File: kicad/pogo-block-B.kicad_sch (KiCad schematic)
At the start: 12 parts, among them J29 MAIN_L, J30 MAIN_R, U61 TL072, U62 TL072

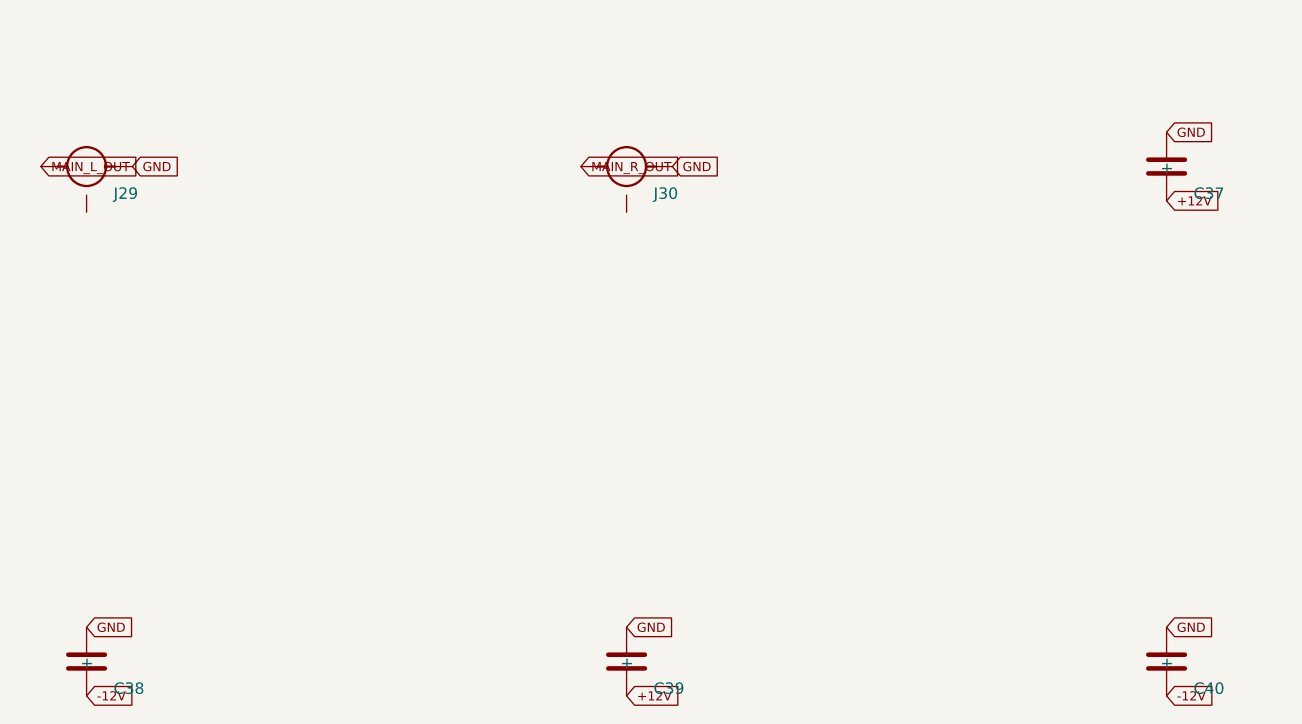
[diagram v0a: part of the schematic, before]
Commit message: 0015-component-audit: apply component verification fixes
Board-breaking:
- that2180: real MPN THAT2180AL08-U (grade A) + package SIP-8 (THT); vendor
  Package_SIP/SIP-8_2.54mm footprint; fix components.yaml U4/U5 + CLAUDE.md.
  The 2180 has no SMD/SOIC variant.
- bat54s: redraw symbol to real series topology (1=A1, 2=K2, 3=K1;A2 junction);
  swap pins 2<->3 on all 24 BAT54S instances (blocks A/1/3/4) so signal sits on the
  junction (pin3), +12V on K2 (pin2), -12V on A1 (pin1); fix aux-cv-protection.md +
  block-A spec (both mislabeled the signal node as pin 2).

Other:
- R_INV_IN/R_INV_FB: add tol 1% (header-required >60 dB null).
- slide_pot_45mm: MPN RA4522F (Alpha 45mm, Rapid/Banzai); fix datasheet link.
- bzx84c10: add shared BZX84_SER datasheet (committed PDF + sha256); canonical MPN.
- opa1612: add symbol opamp2. bourns_3296w/3224w: fix version strings.
- cd4053 symbol doc# -> SCHS047O; c.yaml pin1 '+' -> '~' (non-polarized).

Jack S/T/TN reconciliation deferred (its own change). Plugin DSP untouched.
Regenerated all schematics, BOM, fp-lib-table, footprint SVGs, panel; 5 gates green.
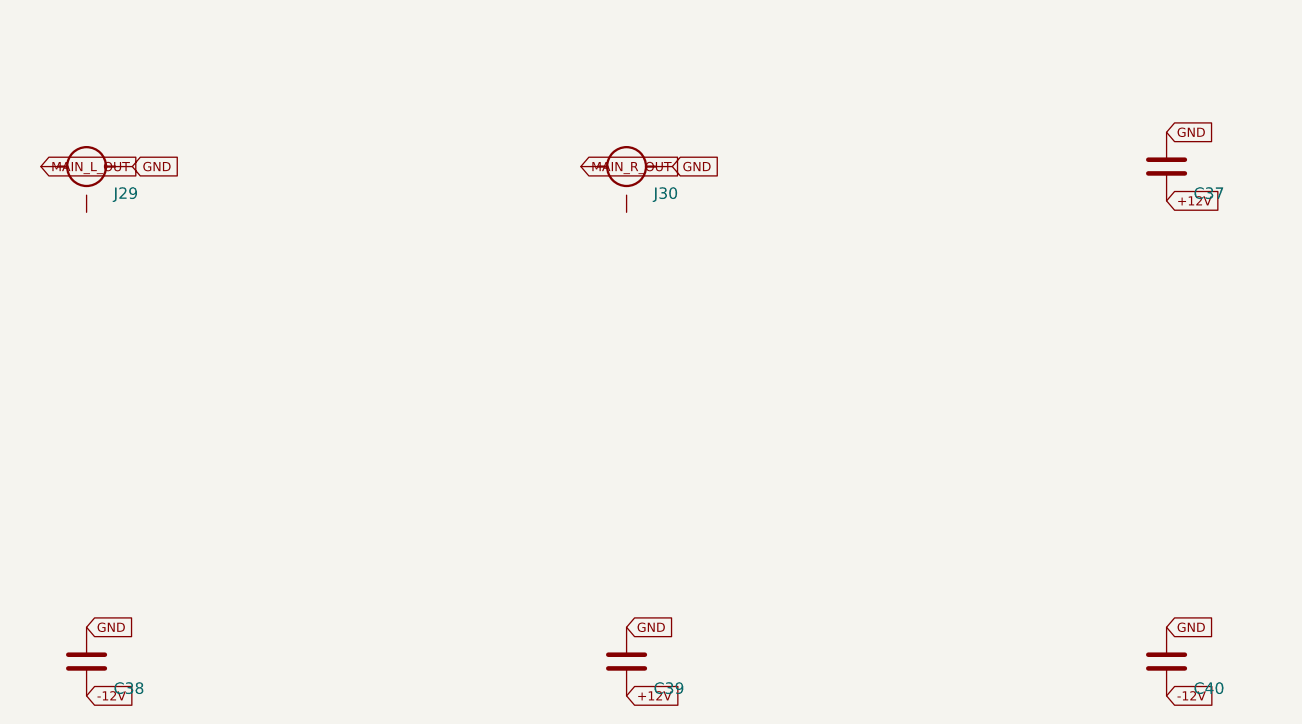
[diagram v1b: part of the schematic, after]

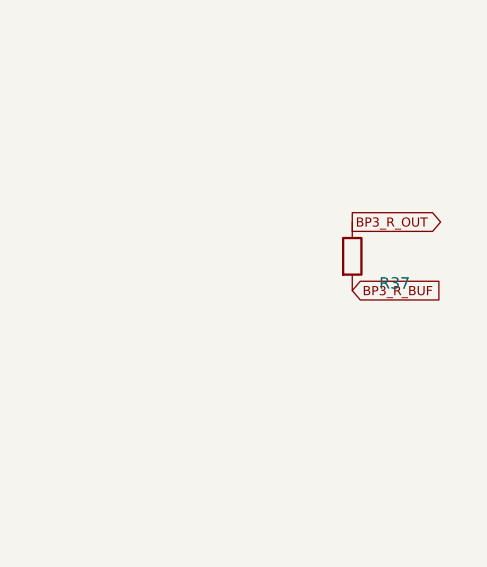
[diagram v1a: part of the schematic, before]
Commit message: 0018: block-B output buffers aligned to plugin (BP3_R normal + hygiene)
Final block. Adversarial review confirmed MAIN outputs faithful (non-inverting
unity followers, 1k series, +-11V via TL072 swing = plugin clamp, like block-A)
and the BP3 tap point correct (svf3 v1, post-bandpass/pre-mix). One real gap:
- BP3_R OUTPUT NORMALLING added: the plugin outputs BP3_L when the BP3_R jack
  is unpatched (Pogo.cpp:498-499). Wired J28.3 (switch lug) -> BP3_L_OUT in
  block-6-mix (which owns the BP3 jacks): BP3_L_OUT: [J27.1, J28.3], J28.3
  removed from no_connect. Mirrors block-A's L->R input normal.
- Renumbered block-B R37 -> R224 to clear the cross-block R37 collision with
  block-3's CV-protection resistors.
- Lifted §2/§3 STALE banners; fixed aux-unity-buffer refs (.svg/.md); noted the
  LFO output resistors are block-2 (utility), editorial in block-B.

All 10 blocks now aligned to the locked plugin. All 5 --check gates + parity green.

https://claude.ai/code/session_013jFXG5oeMVSYP7iRpwGvtQ
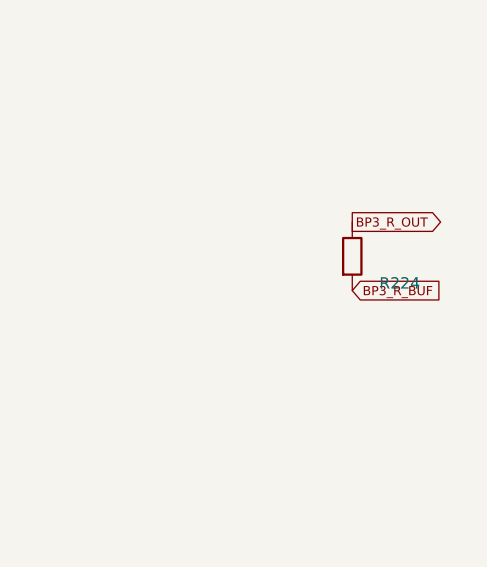
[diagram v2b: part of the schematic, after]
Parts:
- renumbered R37 to R224
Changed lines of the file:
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@@
   (in_bom yes)
   (on_board yes)
-  (property "Reference" "R37" (at 163.000 98.000 0)
+  (property "Reference" "R224" (at 163.000 98.000 0)
     (effects (font (size 1.27 1.27)) (justify left)))
   (property "Value" "1k" (at 163.000 94.500 0)
